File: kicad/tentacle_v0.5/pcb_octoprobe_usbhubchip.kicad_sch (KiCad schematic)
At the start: 35 parts, among them J301 USB_C_Receptacle_USB2.0, U301 AMS1117-3.3, U302 USB2514B_Bi, Y301 24MHz

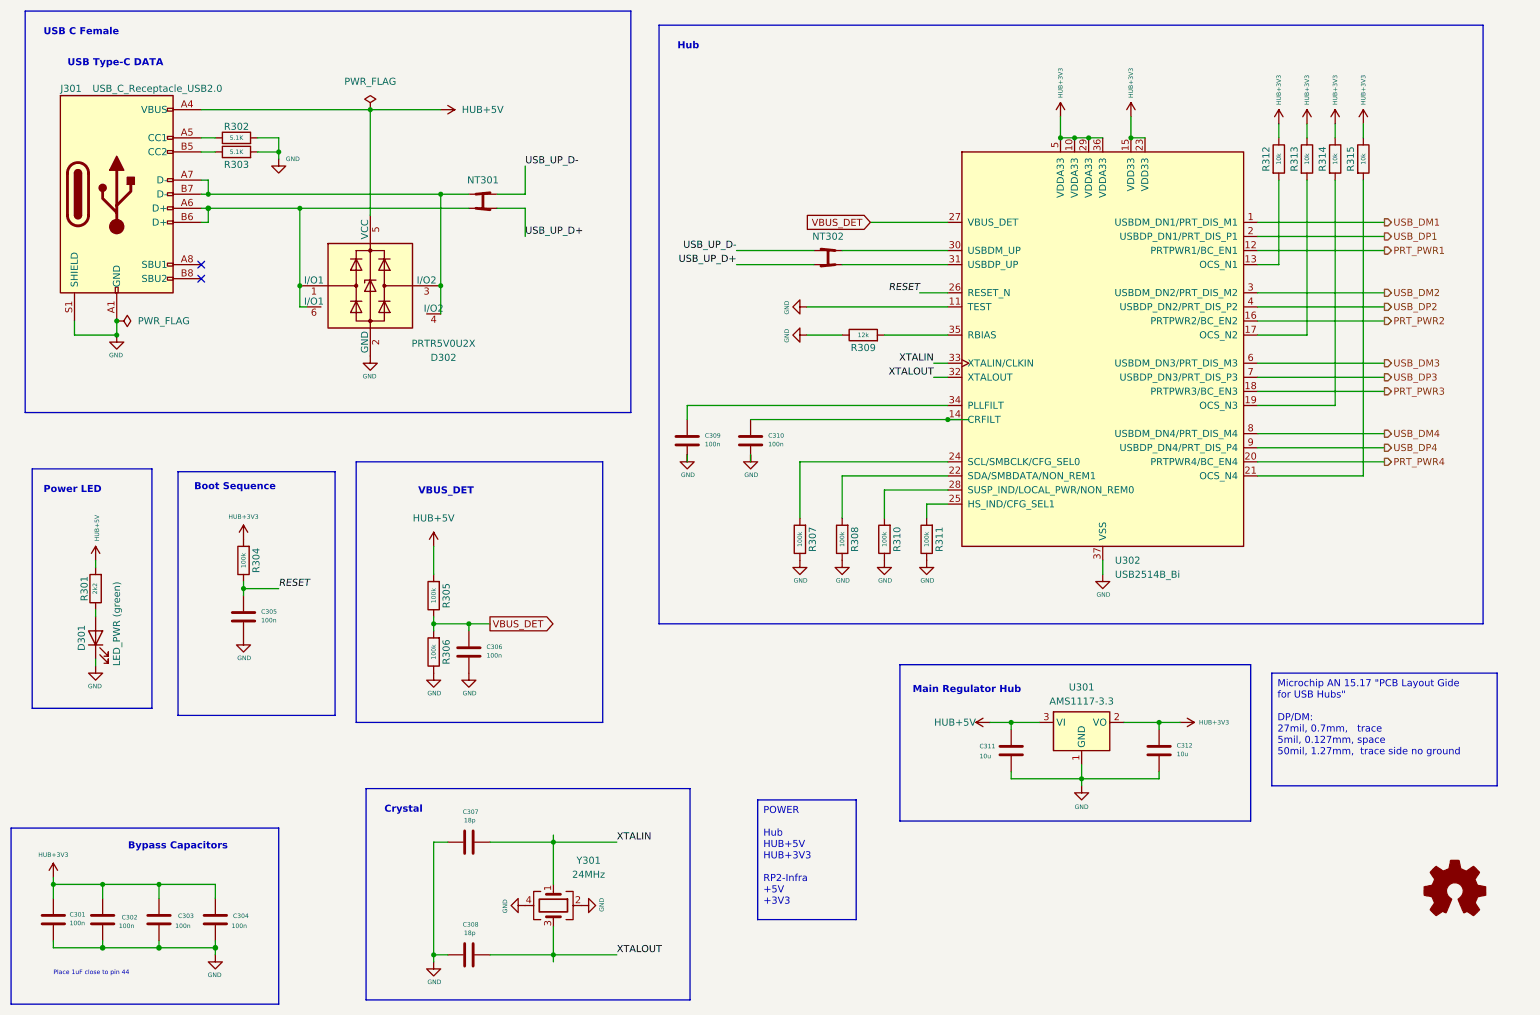
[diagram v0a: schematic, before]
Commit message: Schematics: Fix ERC warnings
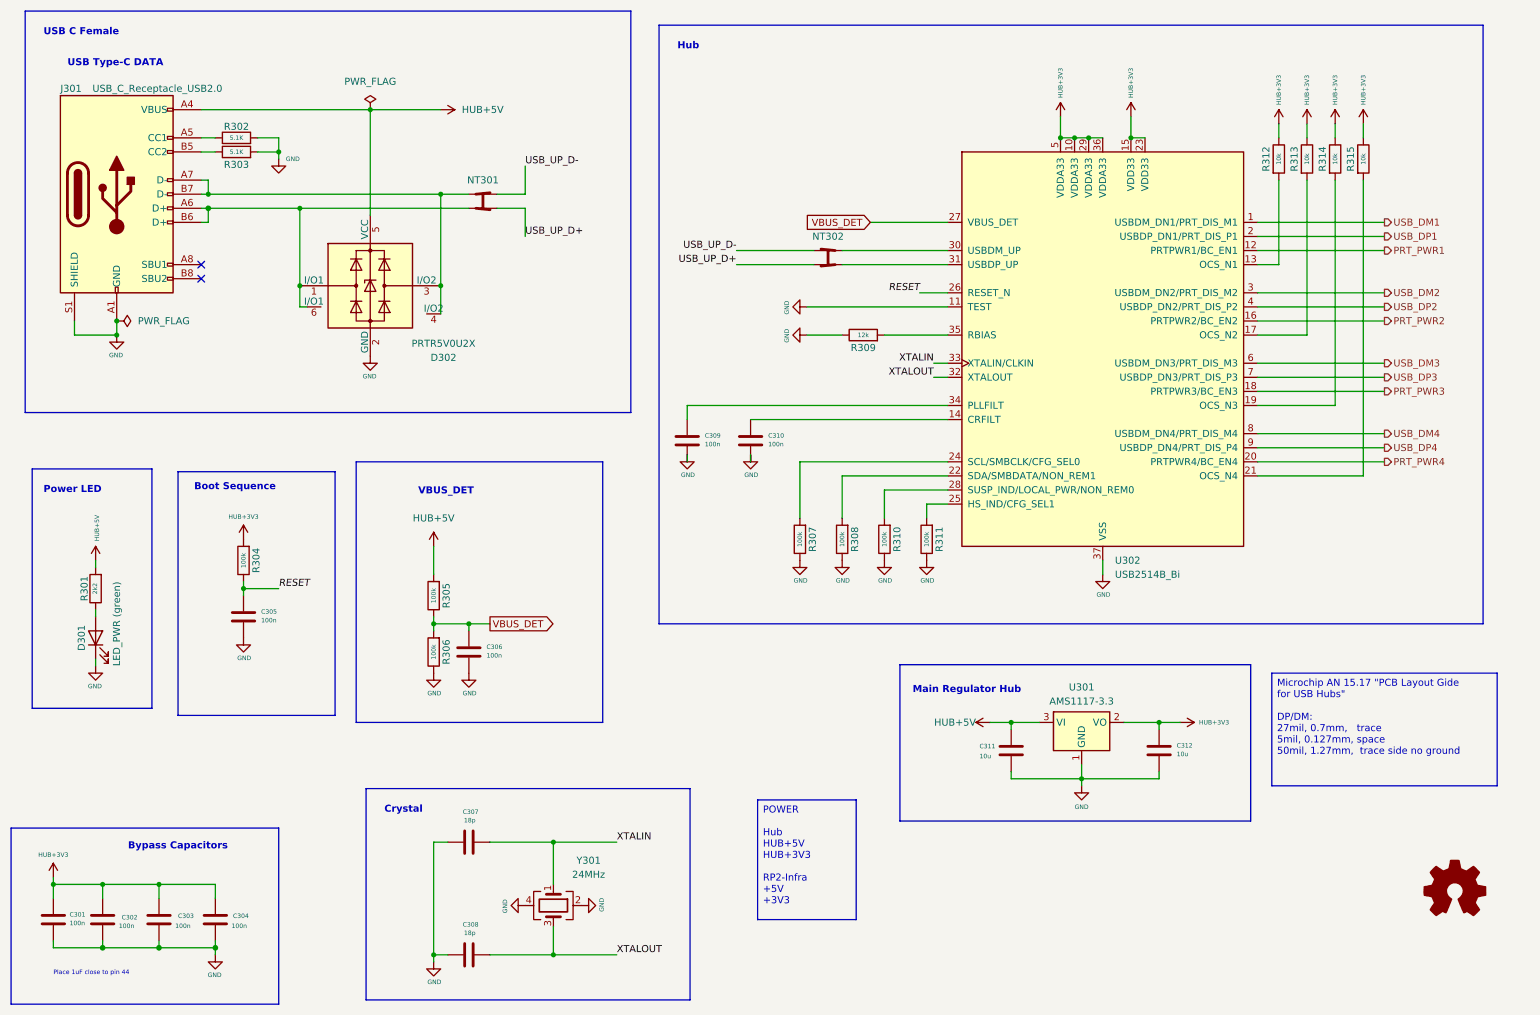
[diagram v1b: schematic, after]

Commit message: Breadboard: Remove pads from schematic
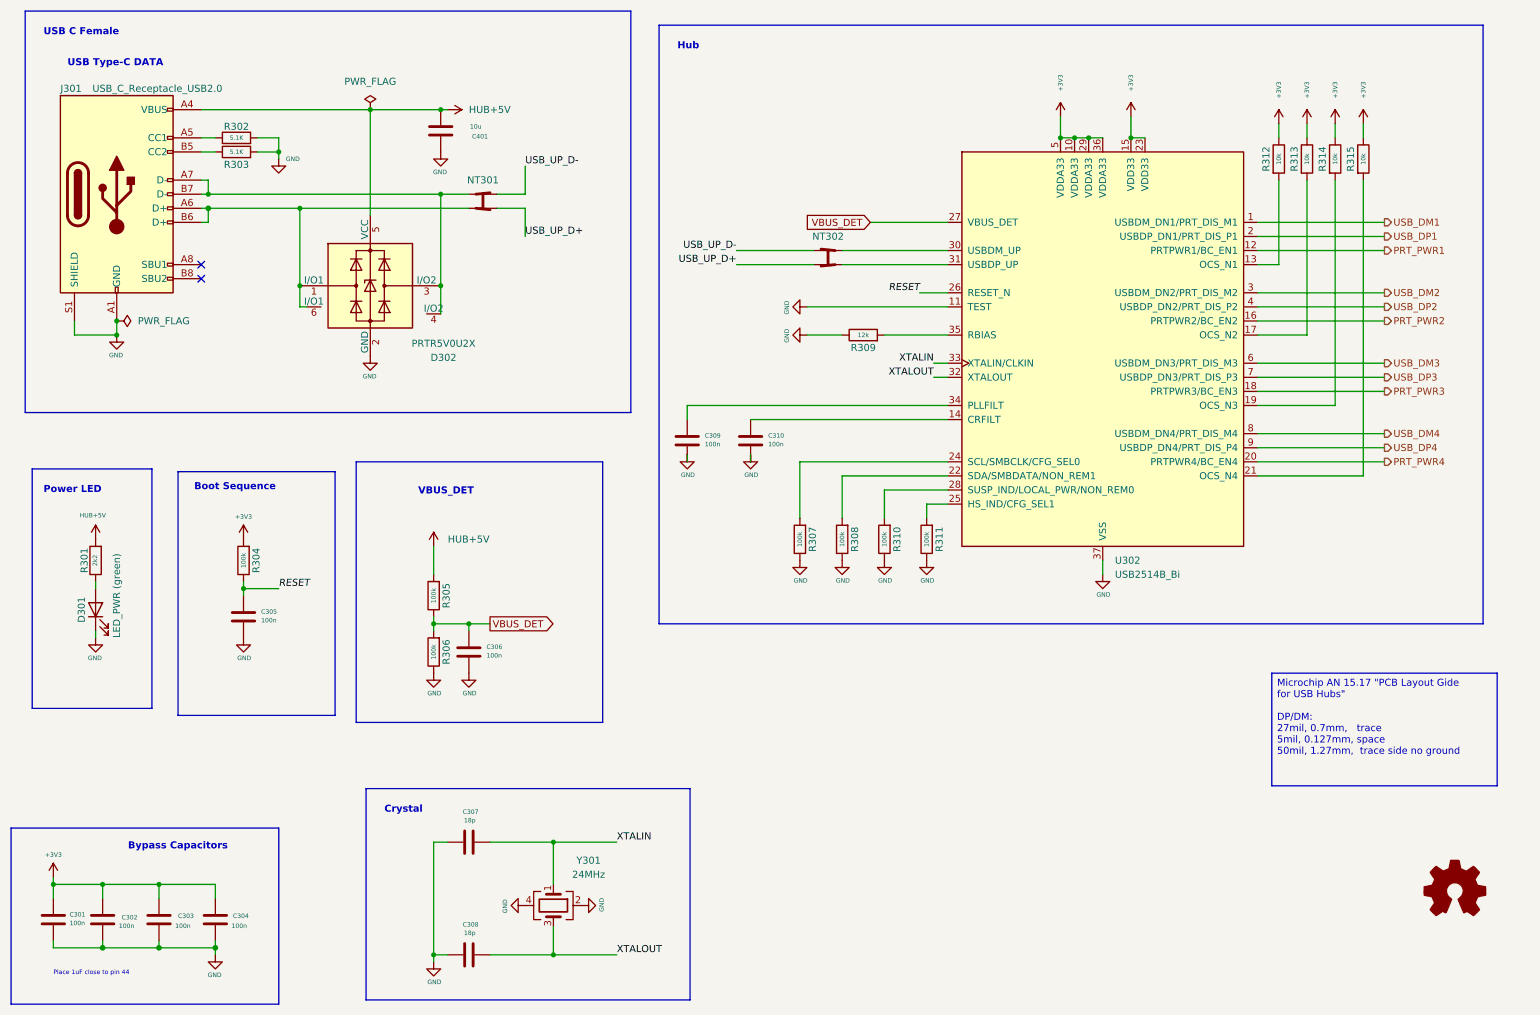
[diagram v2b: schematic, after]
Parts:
- removed C311, C312: 10u, Capacitor_SMD:C_0603_1608Metric, symbol 00_project_library:C
- removed U301: AMS1117-3.3, 00_project_library:SOT-223-3_TabPin2, symbol 00_project_library:AMS1117-3.3
- added C401: 10u, Capacitor_SMD:C_0603_1608Metric, symbol 00_project_library:C
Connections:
- net GND: now also C401.1
- net HUB+5V: now also C401.2
- net HUB+3V3 renamed +3V3
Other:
- note removed: "Main Regulator Hub"
- moved on the sheet: D301, R301

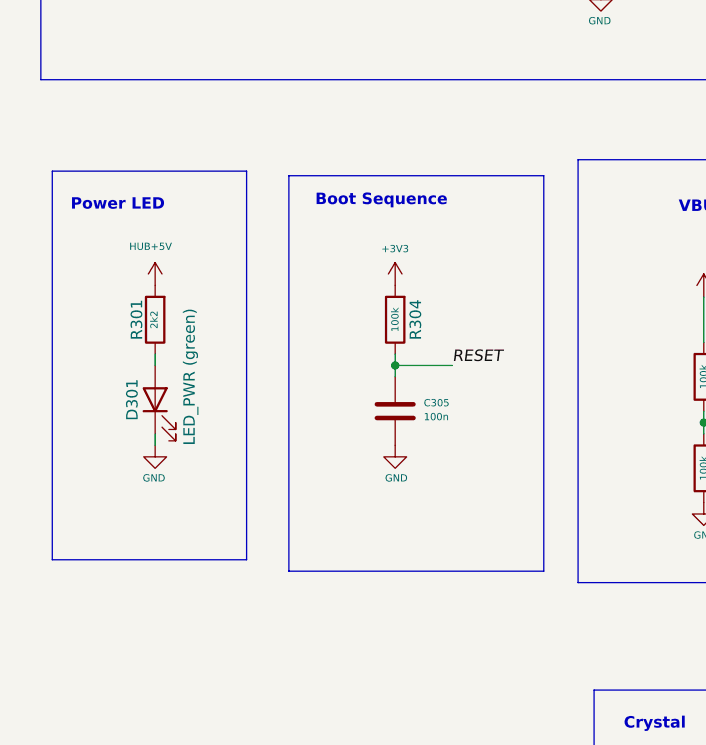
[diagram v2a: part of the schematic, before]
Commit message: ERC and DRC without errors and warnings LEDS less bright (Green LEDs 2k2 -> 4k7)
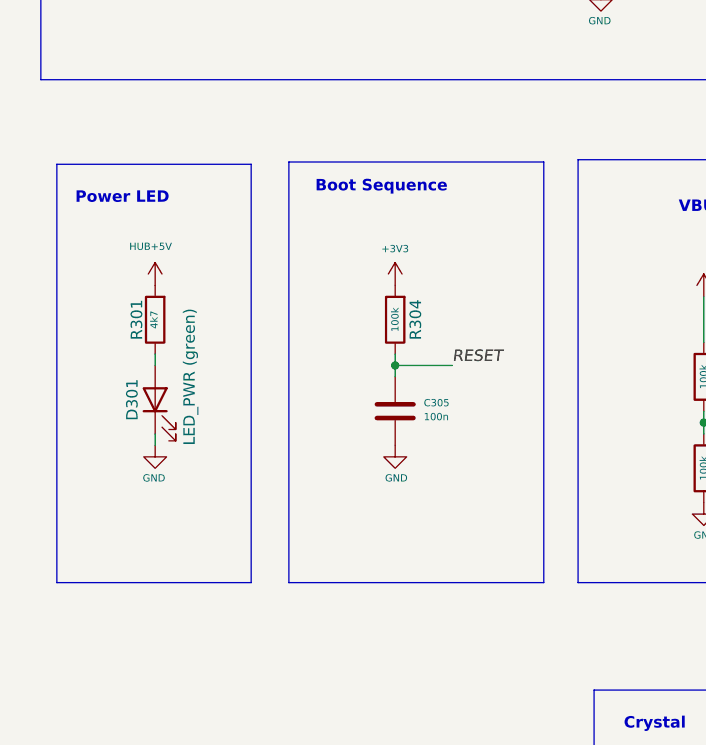
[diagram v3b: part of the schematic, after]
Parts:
- R301: value 2k2 -> 4k7
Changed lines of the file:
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@@
 	)
 	(rectangle
-		(start 45.339 98.298)
-		(end 73.66 142.24)
+		(start 45.339 96.774)
+		(end 73.66 143.51)
 		(stroke
 			(width 0)
@@
 	)
 	(rectangle
-		(start 19.05 97.79)
-		(end 40.64 140.97)
+		(start 19.558 97.028)
+		(end 41.148 143.51)
 		(stroke
 			(width 0)
@@
 	(text "Power LED"
 		(exclude_from_sim no)
-		(at 21.082 102.362 0)
+		(at 21.59 101.6 0)
 		(effects
 			(font
@@
 	(text "Boot Sequence"
 		(exclude_from_sim no)
-		(at 48.26 101.854 0)
+		(at 48.26 100.33 0)
 		(effects
 			(font
@@
 			)
 		)
-		(property "Value" "2k2"
+		(property "Value" "4k7"
 			(at 30.3784 114.3 90)
 			(effects
@@
 			)
 		)
-		(property "Description" ""
+		(property "Description" "USB 2.0-only Type-C Receptacle connector"
 			(at 34.29 48.26 0)
 			(effects

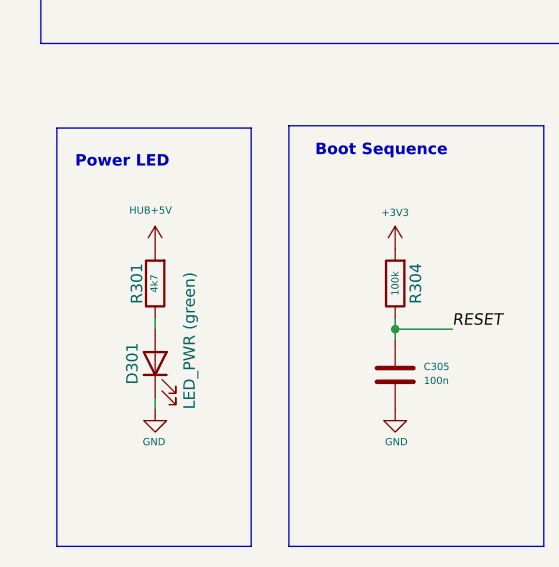
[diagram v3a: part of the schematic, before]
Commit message: Ordered tentacle v0.5 at jlcpcb
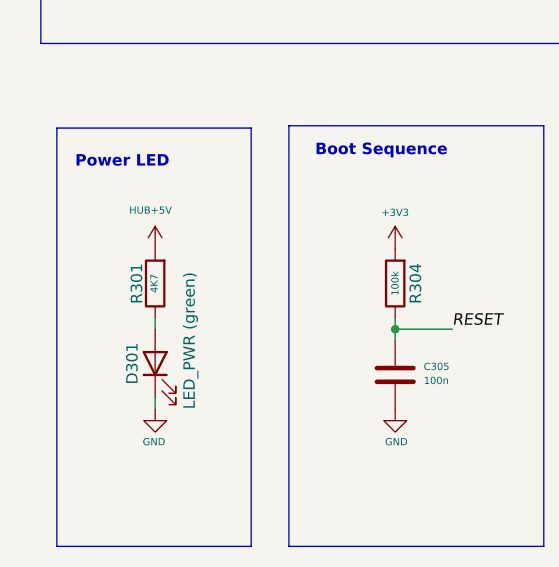
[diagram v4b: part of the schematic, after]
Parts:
- R301: value 4k7 -> 4K7
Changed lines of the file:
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@@
 	(title_block
 		(title "Octoprobe tentacle")
-		(date "2025-09-02")
+		(date "2025-08-31")
 		(rev "0.5")
 		(company "Hans Märki, Märki Informatik")
@@
 			)
 		)
-		(property "Value" "4k7"
+		(property "Value" "4K7"
 			(at 30.3784 114.3 90)
 			(effects
